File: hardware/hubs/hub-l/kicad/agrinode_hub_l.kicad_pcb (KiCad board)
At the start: 2 copper layers, 130 x 96 mm, 105 parts, among them J1 DC 12V 5.5/2.1, J2 DC IN 7-24V, J3 SOLAR 6-24V, J4 USB 5V / PROG, J5 BAT NTC 10k, J6 PROG, J7 I2C, J8 LED STRIP WS2813, J9 RS-485, Q1 AO3401A, Q2 AO3401A, Q3 MMBT3904, Q4 MMBT3904, Q5 BSS138, Q6 MMBT3904, SW1 RESET, SW2 BOOT / PAIR, U1 LM2596S-5.0, U2 TP4056, U3 MIC29302WU, U4 ESP32-WROOM-32E-N8, U5 CH340C, U6 DS3231MZ, U7 MAX3485ESA, U8 Ra-02 SX1278 433MHz

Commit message: hubs: routing progress snapshot
Co-Authored-By: Claude Opus 5.5 <noreply@anthropic.com>
Claude-Session: https://claude.ai/code/session_014J7amXZ5Y6AZWEh5CjDNja
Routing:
- net GND: track 0.00 -> 848.0 mm, vias 0 -> 10
- net +3V3: track 0.00 -> 359.7 mm, vias 0 -> 7
- net /Power - 12V, solar and USB inputs, 18650 charger, rails/V5: track 0.00 -> 166.6 mm, vias 0 -> 5
- net /Power - 12V, solar and USB inputs, 18650 charger, rails/VUSB_RAW: track 0.00 -> 166.0 mm, vias 0 -> 3
- net VSYS: track 0.00 -> 165.3 mm, vias 0 -> 5
- net LORA_CS: track 0.00 -> 108.7 mm, vias 0 -> 5
- net LORA_RST: track 0.00 -> 104.2 mm, vias 0 -> 4
- net /ESP32, programming, buttons, RTC, LED strip, buzzer/ESP_EN: track 0.00 -> 100.7 mm, vias 0 -> 4
- net SPI_SCK: track 0.00 -> 97.9 mm, vias 0 -> 6
- net SPI_MOSI: track 0.00 -> 97.0 mm, vias 0 -> 4
- net /Power - 12V, solar and USB inputs, 18650 charger, rails/VIN_BUCK: track 0.00 -> 95.2 mm, vias 0 -> 3
- net /ESP32, programming, buttons, RTC, LED strip, buzzer/I2C_SCL: track 0.00 -> 91.7 mm, vias 0 -> 2
- net /Power - 12V, solar and USB inputs, 18650 charger, rails/BATT_CELL: track 0.00 -> 90.6 mm, vias 0 -> 2
- net /ESP32, programming, buttons, RTC, LED strip, buzzer/BOOT_BTN: track 0.00 -> 89.1 mm, vias 0 -> 1
- net /ESP32, programming, buttons, RTC, LED strip, buzzer/I2C_SDA: track 0.00 -> 88.5 mm, vias 0 -> 2
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- added copper zone on B.Cu, net GND
- added copper zone on F.Cu, net GND

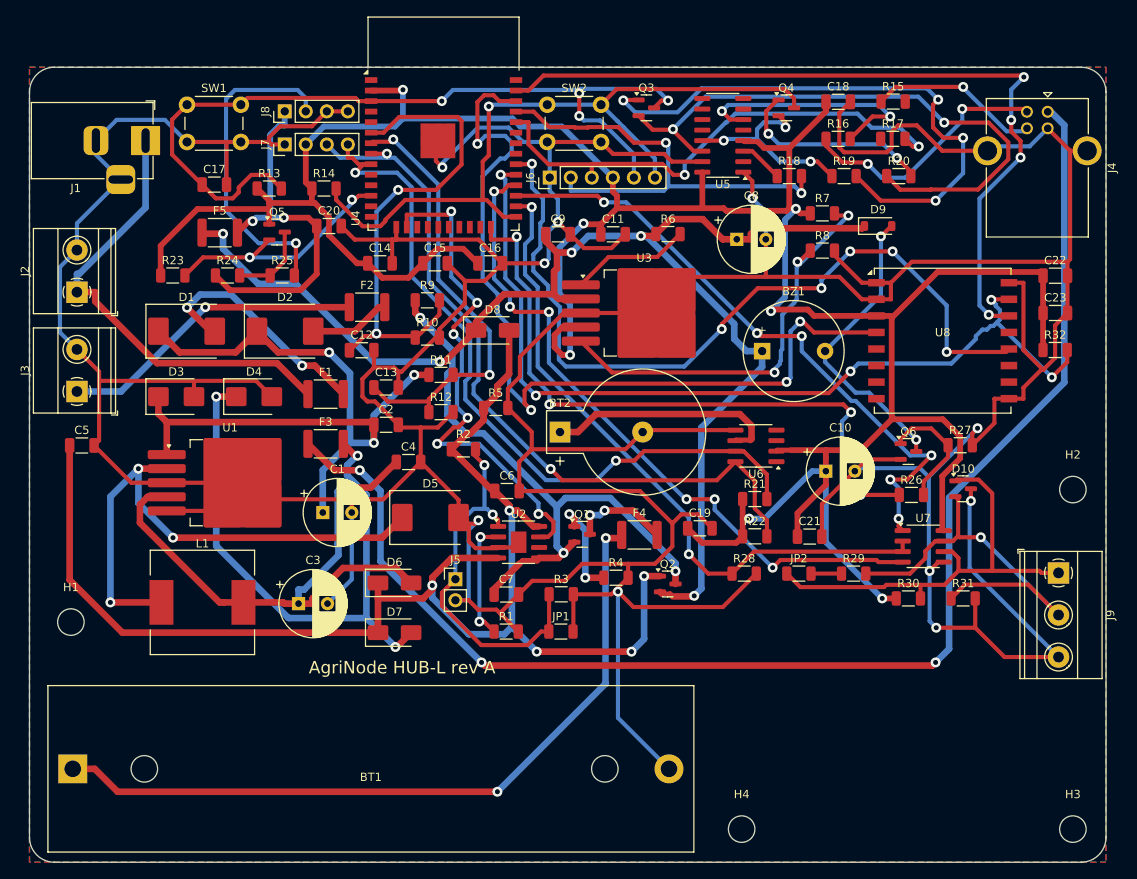
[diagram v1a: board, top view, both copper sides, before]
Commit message: hubs: open a 6 mm routing channel beside the ESP32 right column (BOOT button and PROG header moved); pin the LDO bulk cap
Co-Authored-By: Claude Opus 5.5 <noreply@anthropic.com>
Claude-Session: https://claude.ai/code/session_014J7amXZ5Y6AZWEh5CjDNja
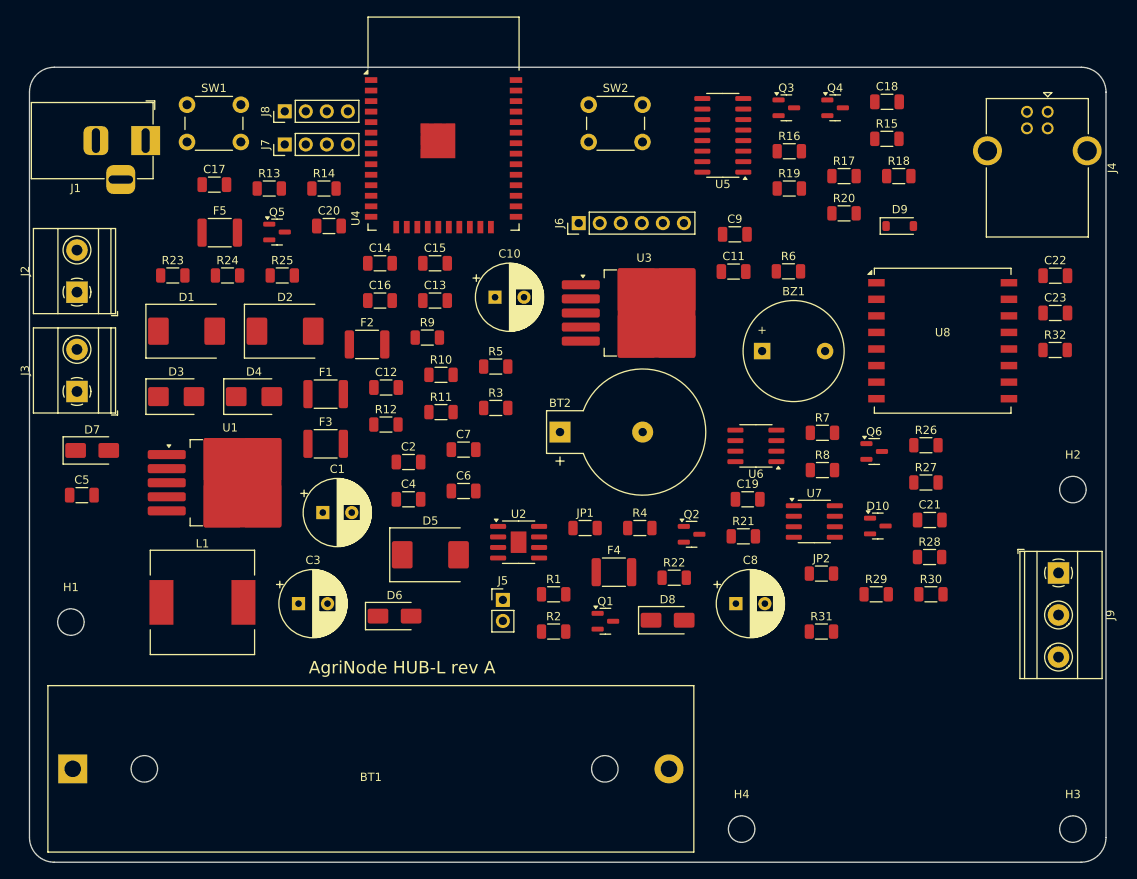
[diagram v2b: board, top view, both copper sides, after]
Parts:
- moved C10 45.1 mm to (106.2, 77.8)
- moved C8 44.0 mm to (135.3, 114.8)
- moved D7 42.6 mm to (57.6, 96.3)
- moved D8 40.9 mm to (127.1, 116.8)
- moved R7 26.5 mm to (145.8, 94.1)
- moved R8 26.5 mm to (145.8, 98.6)
- moved R2 24.5 mm to (113.3, 118.1)
- moved R3 23.8 mm to (106.3, 91.1)
- moved R28 22.5 mm to (158.7, 109.1)
- moved C9 21.4 mm to (135.2, 70.2)
- moved C7 18.2 mm to (102.4, 96.2)
- moved R31 17.6 mm to (145.6, 118.1)
- moved Q3 16.9 mm to (141.4, 54.9)
- moved R6 15.2 mm to (141.7, 74.6)
- moved C11 15.2 mm to (135.0, 74.7)
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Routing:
- net GND: track 848.0 -> 0.00 mm, vias 10 -> 0
- net +3V3: track 359.7 -> 0.00 mm, vias 7 -> 0
- net /Power - 12V, solar and USB inputs, 18650 charger, rails/V5: track 166.6 -> 0.00 mm, vias 5 -> 0
- net /Power - 12V, solar and USB inputs, 18650 charger, rails/VUSB_RAW: track 166.0 -> 0.00 mm, vias 3 -> 0
- net VSYS: track 165.3 -> 0.00 mm, vias 5 -> 0
- net LORA_CS: track 108.7 -> 0.00 mm, vias 5 -> 0
- net LORA_RST: track 104.2 -> 0.00 mm, vias 4 -> 0
- net /ESP32, programming, buttons, RTC, LED strip, buzzer/ESP_EN: track 100.7 -> 0.00 mm, vias 4 -> 0
- net SPI_SCK: track 97.9 -> 0.00 mm, vias 6 -> 0
- net SPI_MOSI: track 97.0 -> 0.00 mm, vias 4 -> 0
- net /Power - 12V, solar and USB inputs, 18650 charger, rails/VIN_BUCK: track 95.2 -> 0.00 mm, vias 3 -> 0
- net /ESP32, programming, buttons, RTC, LED strip, buzzer/I2C_SCL: track 91.7 -> 0.00 mm, vias 2 -> 0
- net /Power - 12V, solar and USB inputs, 18650 charger, rails/BATT_CELL: track 90.6 -> 0.00 mm, vias 2 -> 0
- net /ESP32, programming, buttons, RTC, LED strip, buzzer/BOOT_BTN: track 89.1 -> 0.00 mm, vias 1 -> 0
- net /ESP32, programming, buttons, RTC, LED strip, buzzer/I2C_SDA: track 88.5 -> 0.00 mm, vias 2 -> 0
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- removed copper zone on B.Cu, net GND
- removed copper zone on F.Cu, net GND

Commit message: hubs: GND stitching vias + GND left to the pours (autorouter routes signals only)
Co-Authored-By: Claude Opus 5.5 <noreply@anthropic.com>
Claude-Session: https://claude.ai/code/session_014J7amXZ5Y6AZWEh5CjDNja
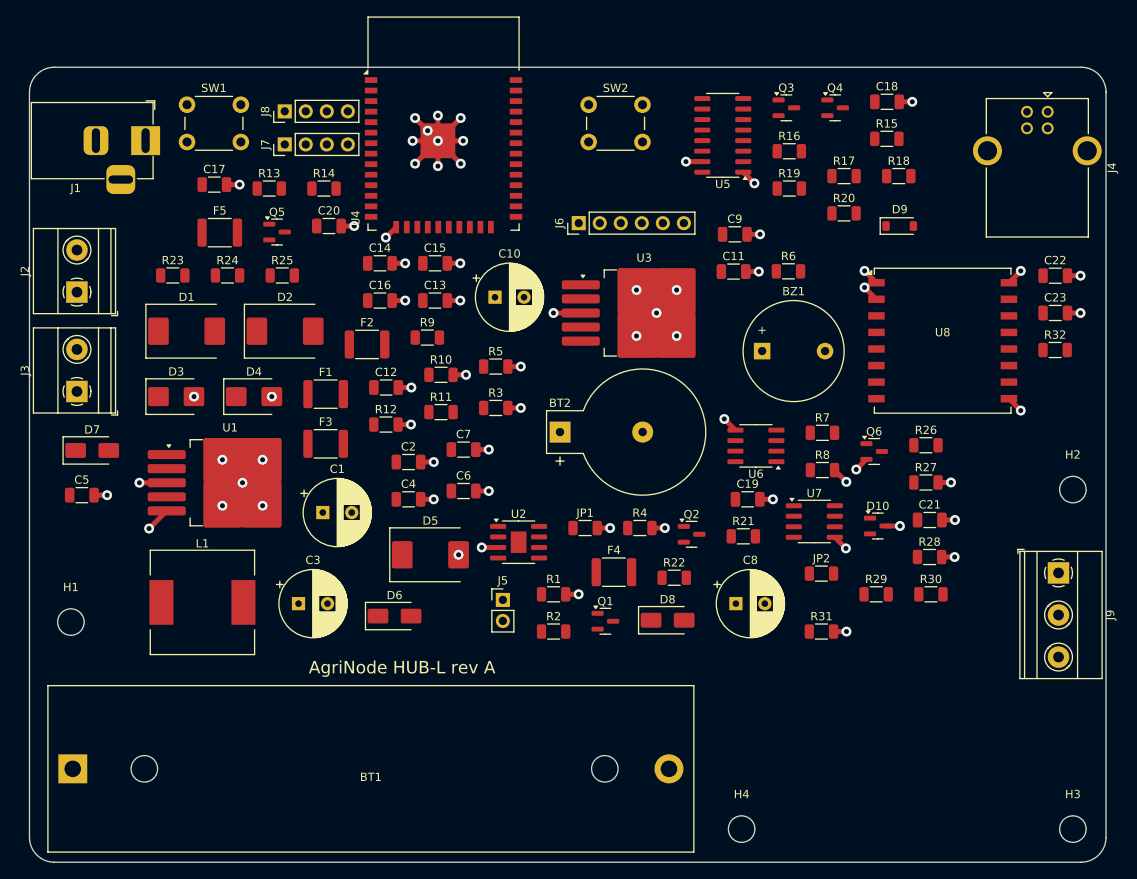
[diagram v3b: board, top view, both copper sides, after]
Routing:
- net GND: track 0.00 -> 95.0 mm, vias 0 -> 68

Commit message: hubs: keep HUB-W on its fully routed layout (routing-channel moves only for the other variants); GND stitching off by default
Co-Authored-By: Claude Opus 5.5 <noreply@anthropic.com>
Claude-Session: https://claude.ai/code/session_014J7amXZ5Y6AZWEh5CjDNja
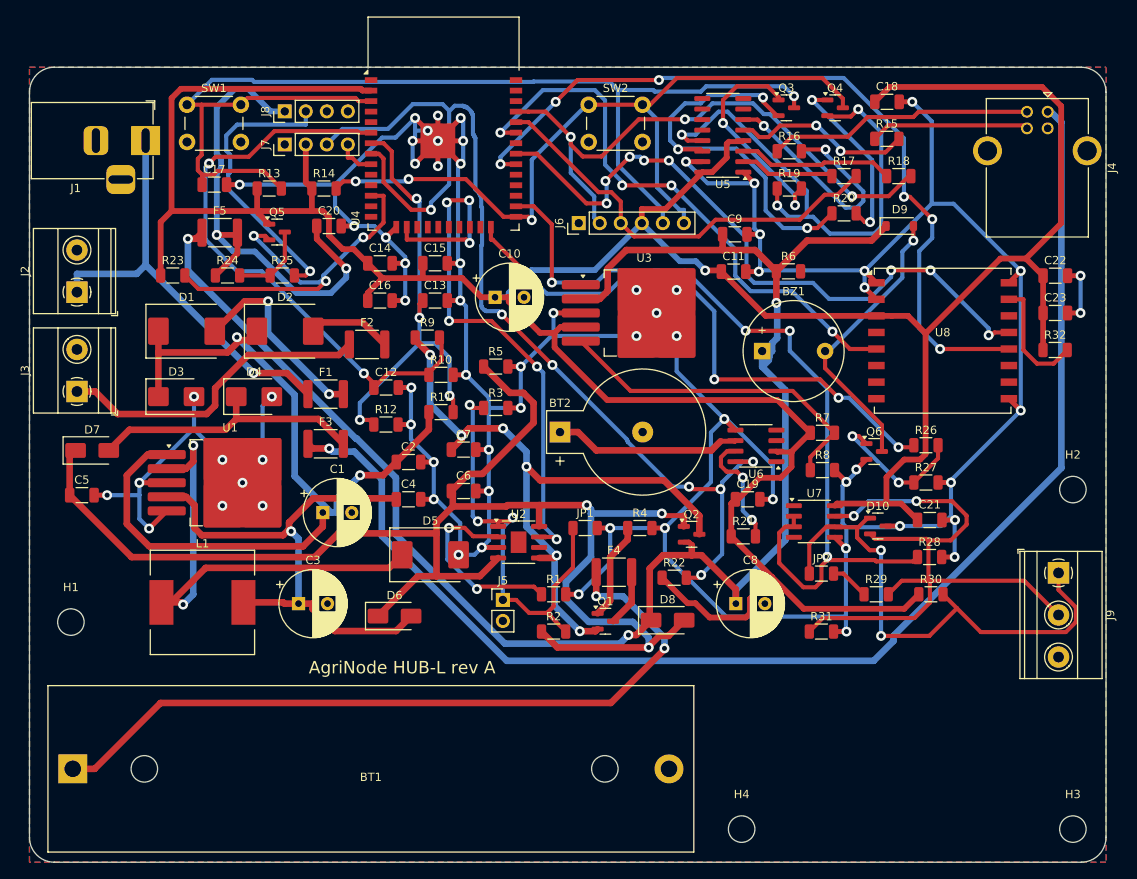
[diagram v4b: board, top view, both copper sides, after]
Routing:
- net GND: track 95.0 -> 554.7 mm
- net +3V3: track 0.00 -> 411.2 mm, vias 0 -> 1
- net VSYS: track 0.00 -> 201.4 mm, vias 0 -> 3
- net /Power - 12V, solar and USB inputs, 18650 charger, rails/V5: track 0.00 -> 183.3 mm, vias 0 -> 3
- net /Power - 12V, solar and USB inputs, 18650 charger, rails/VUSB_RAW: track 0.00 -> 159.8 mm, vias 0 -> 1
- net /ESP32, programming, buttons, RTC, LED strip, buzzer/ESP_EN: track 0.00 -> 139.1 mm, vias 0 -> 1
- net /ESP32, programming, buttons, RTC, LED strip, buzzer/I2C_SCL: track 0.00 -> 128.1 mm, vias 0 -> 7
- net /Power - 12V, solar and USB inputs, 18650 charger, rails/VIN_BUCK: track 0.00 -> 106.5 mm, vias 0 -> 2
- net RS485_DE: track 0.00 -> 101.8 mm, vias 0 -> 4
- net SPI_SCK: track 0.00 -> 95.7 mm, vias 0 -> 6
- net /ESP32, programming, buttons, RTC, LED strip, buzzer/BOOT_BTN: track 0.00 -> 93.9 mm, vias 0 -> 3
- net /Power - 12V, solar and USB inputs, 18650 charger, rails/BATT_CELL: track 0.00 -> 92.1 mm, vias 0 -> 2
- net SPI_MISO: track 0.00 -> 81.6 mm, vias 0 -> 8
- net /Power - 12V, solar and USB inputs, 18650 charger, rails/VBAT: track 0.00 -> 80.4 mm, vias 0 -> 6
- net /RS-485 and uplink/RS485_B: track 0.00 -> 77.7 mm, vias 0 -> 2
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- added copper zone on B.Cu, net GND
- added copper zone on F.Cu, net GND

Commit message: hubs: routing progress snapshot
Co-Authored-By: Claude Opus 5.5 <noreply@anthropic.com>
Claude-Session: https://claude.ai/code/session_014J7amXZ5Y6AZWEh5CjDNja
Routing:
- net GND: track 554.7 -> 0.00 mm, vias 68 -> 0
- net +3V3: track 411.2 -> 0.00 mm, vias 1 -> 0
- net VSYS: track 201.4 -> 0.00 mm, vias 3 -> 0
- net /Power - 12V, solar and USB inputs, 18650 charger, rails/V5: track 183.3 -> 0.00 mm, vias 3 -> 0
- net /Power - 12V, solar and USB inputs, 18650 charger, rails/VUSB_RAW: track 159.8 -> 0.00 mm, vias 1 -> 0
- net /ESP32, programming, buttons, RTC, LED strip, buzzer/ESP_EN: track 139.1 -> 0.00 mm, vias 1 -> 0
- net /ESP32, programming, buttons, RTC, LED strip, buzzer/I2C_SCL: track 128.1 -> 0.00 mm, vias 7 -> 0
- net /Power - 12V, solar and USB inputs, 18650 charger, rails/VIN_BUCK: track 106.5 -> 0.00 mm, vias 2 -> 0
- net RS485_DE: track 101.8 -> 0.00 mm, vias 4 -> 0
- net SPI_SCK: track 95.7 -> 0.00 mm, vias 6 -> 0
- net /ESP32, programming, buttons, RTC, LED strip, buzzer/BOOT_BTN: track 93.9 -> 0.00 mm, vias 3 -> 0
- net /Power - 12V, solar and USB inputs, 18650 charger, rails/BATT_CELL: track 92.1 -> 0.00 mm, vias 2 -> 0
- net SPI_MISO: track 81.6 -> 0.00 mm, vias 8 -> 0
- net /Power - 12V, solar and USB inputs, 18650 charger, rails/VBAT: track 80.4 -> 0.00 mm, vias 6 -> 0
- net /RS-485 and uplink/RS485_B: track 77.7 -> 0.00 mm, vias 2 -> 0
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- removed copper zone on B.Cu, net GND
- removed copper zone on F.Cu, net GND
